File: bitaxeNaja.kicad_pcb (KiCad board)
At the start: 6 copper layers, 65 x 112 mm, 197 parts, among them J1 XT30, J2 Conn_01x08, J3 Conn_01x04, J4 USB_C_Receptacle_USB2.0, J7 Conn_01x04, J8 TC2030-IDC, SW1 SWITCH-SPST, SW2 SWITCH-SPST, U1 TPS546D24ARVFR, U10 BM1370_mode1, U11 MCP1824T-1202E/OT, U12 MCP1824T-0802E, U13 EMC2103-2, U2 SN74AVC4T774, U3 TPSM861253RDXR, U4 TPS546D24ARVFR, U5 L78L05_SOT89, U6 ESP32-S3-WROOM-1, U8 25MHz, U9 BM1370_mode1

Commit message: lots of routing
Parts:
- removed the G*** at (130.5, 70.7)
- removed R10, R12, R9: R, Resistor_SMD:R_0402_1005Metric
- added R41: 38.3k, Resistor_SMD:R_0402_1005Metric, B.Cu at (132.9, 115.1)
- added R42: 20k, Resistor_SMD:R_0402_1005Metric, B.Cu at (131.8, 115.1)
- added R43: 19.1k, Resistor_SMD:R_0402_1005Metric, B.Cu at (129.1, 115.1)
- added R44: 20k, Resistor_SMD:R_0402_1005Metric, B.Cu at (128.0, 115.1)
- A1: renamed from U9; value BM1370_mode1 -> BM1340_mode1; footprint bitaxe:BM1370 -> bitaxe:BM1340
- A2: renamed from U10; value BM1370_mode1 -> BM1340_mode1; footprint bitaxe:BM1370 -> bitaxe:BM1340
- U11: value MCP1824T-1202E/OT -> MCP1824
- U12: value MCP1824T-0802E -> MCP1824
- moved TP27 31.4 mm to (95.7, 55.8)
- moved TP32 30.9 mm to (114.7, 39.3)
- moved TP33 29.2 mm to (110.6, 39.3)
- moved FID1 10.5 mm to (100.4, 32.2)
- moved C88 8.38 mm to (133.5, 121.4), turned to 0 degrees
- moved TP18 8.19 mm to (132.9, 112.3)
- moved C90 7.45 mm to (129.6, 121.3), turned to 0 degrees
- moved TP19 6.76 mm to (129.1, 112.3)
- moved R6 6.31 mm to (126.2, 54.9), turned to 0 degrees
- moved R13 6.27 mm to (146.7, 78.8), turned to 90 degrees
- moved C89 6.21 mm to (134.0, 115.1), turned to -90 degrees
- moved R21 6.13 mm to (126.2, 56.1), turned to 180 degrees
- moved TP4 5.30 mm to (103.8, 110.8)
- moved U11 5.16 mm to (133.0, 118.6), turned to 90 degrees
- moved R11 5.01 mm to (147.9, 78.8), turned to -90 degrees
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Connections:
- U1 pad 29: Net-(U1-MSEL2) -> unconnected-(U1-MSEL2-Pad29)
- U11 pad 4: unconnected-(U11-PG-Pad4) -> Net-(U11-ADJ)
- U12 pad 4: unconnected-(U12-PG-Pad4) -> Net-(U12-ADJ)
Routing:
- net GND: track 98.4 -> 69.7 mm, vias 332 -> 238
- net Net-(U1-MSEL2): track 27.7 -> 0.00 mm, vias 2 -> 0
- net /5V: track 184.2 -> 161.8 mm, vias 9 -> 11
- net /Power/ALRT_VR: track 54.5 -> 66.9 mm, vias 4 -> 3
- net /3V3: track 145.5 -> 134.3 mm
- net /ESP32/IO0: track 91.2 -> 81.9 mm
- net /Power/AGND2: track 30.9 -> 40.1 mm, vias 4 -> 3
- net Net-(U1-VSEL): track 25.8 -> 17.2 mm
- net /ASIC/TEMP2_N: track 36.3 -> 27.8 mm
- net Net-(A1-INV_CLKO): track 14.2 -> 7.18 mm
- net /ASIC/TEMP1_P: track 26.0 -> 33.0 mm
- net Net-(A1-LITE_PAD): track 13.0 -> 6.14 mm
- net /ASIC/TEMP1_N: track 24.6 -> 31.4 mm
- net /ASIC/TEMP2_P: track 33.2 -> 26.4 mm
- net /ASIC/1V2: track 114.9 -> 108.1 mm, vias 7 -> 6
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- removed copper zone on In2.Cu, net /Power/AGND1
- removed copper zone on In2.Cu, net /Power/AGND2
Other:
- board text added: "1200x"
- board text removed: "800xxx"

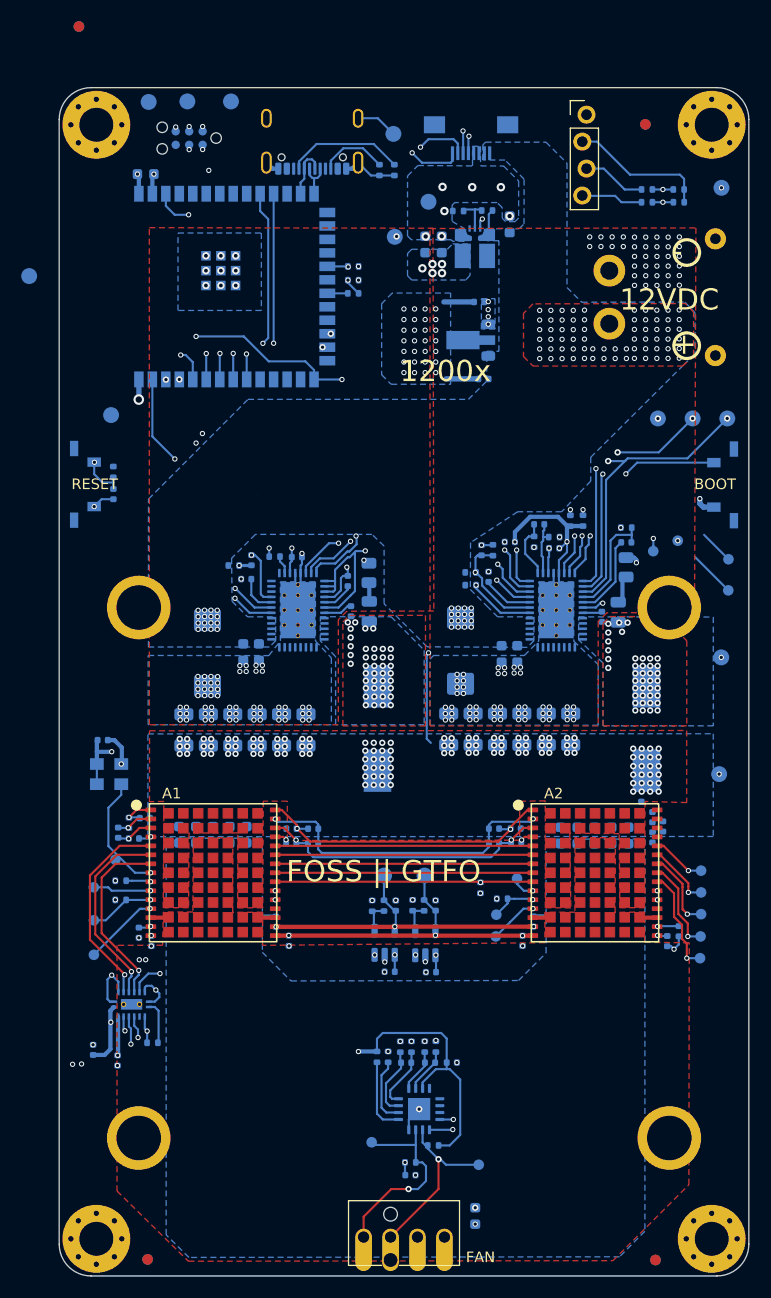
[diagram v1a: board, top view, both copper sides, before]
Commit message: placed and routed and DRC'd. updated TPS546 for 1.0V output.
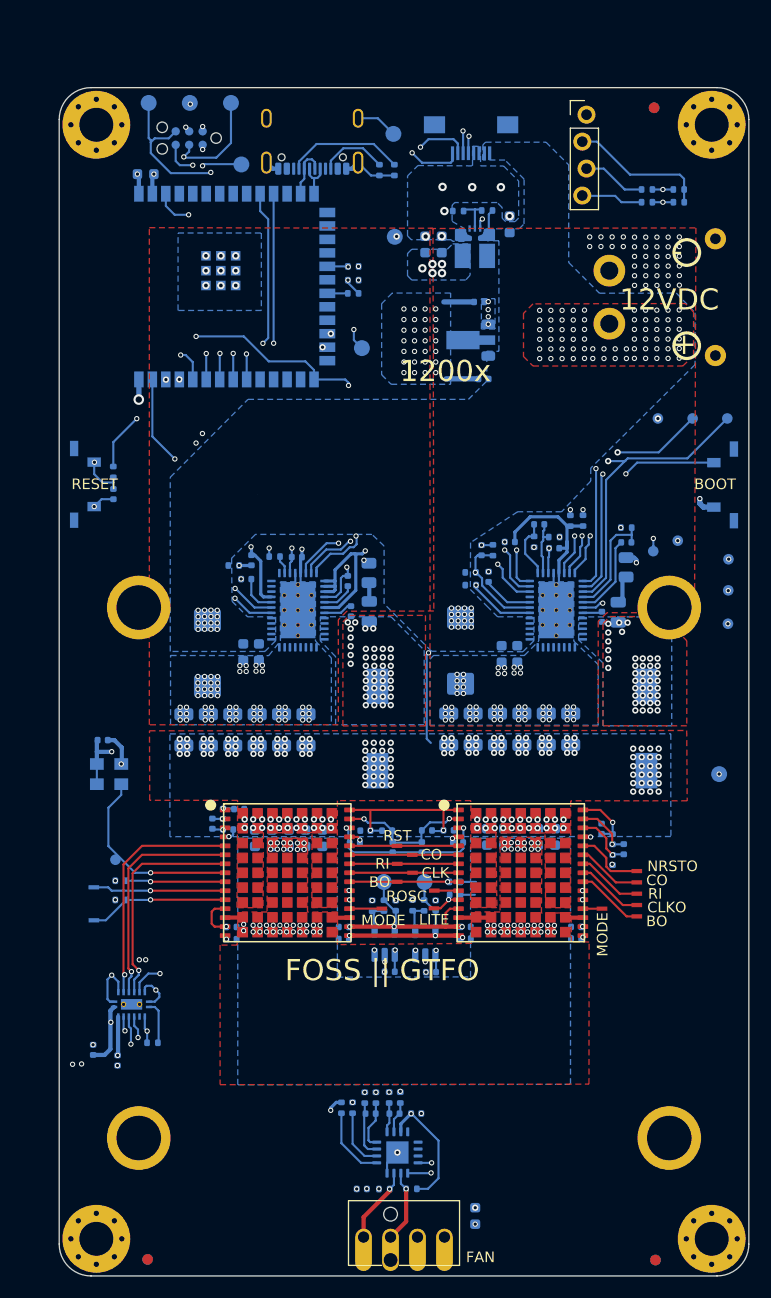
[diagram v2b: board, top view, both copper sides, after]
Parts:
- removed FID1: Fiducial, bitaxe:Fiducial_1mm_Mask2mm
- removed TP14, TP16, TP20, TP21: TestPoint, TestPoint:TestPoint_Pad_D1.0mm
- removed TP17, TP28: GND, TestPoint:TestPoint_Pad_D1.5mm
- added TP26: RST, bitaxe:TestPoint_Pad_1.0x0.4mm, F.Cu at (130.3, 109.5)
- added TP37: CO, bitaxe:TestPoint_Pad_1.0x0.4mm, F.Cu at (131.8, 110.3)
- added TP38: RI, bitaxe:TestPoint_Pad_1.0x0.4mm, F.Cu at (130.4, 111.2)
- added TP39: CLK, bitaxe:TestPoint_Pad_1.0x0.4mm, F.Cu at (131.8, 112.0)
- added TP40: BO, bitaxe:TestPoint_Pad_1.0x0.4mm, F.Cu at (130.4, 112.8)
- added TP41: MODE, bitaxe:TestPoint_Pad_1.0x0.4mm, F.Cu at (128.9, 115.4)
- added TP42: MODE, bitaxe:TestPoint_Pad_1.0x0.4mm, F.Cu at (149.7, 115.4)
- L1, L2: value 300nH -> 230nH; footprint bitaxe:SLC1175-271MEC_COC -> bitaxe:FP1107R1
- R11: value 14.7k -> 46.4k
- R13: value 56.2k -> 31.6k
- R4: value 75k -> 6.04k
- R5: value 10k -> 649
- R7: value 14.7k -> 31.6k
- TP10: value TestPoint -> ROSC; footprint TestPoint:TestPoint_Pad_D1.0mm -> bitaxe:TestPoint_Pad_1.0x0.4mm
- TP11: value TestPoint -> ROSC; footprint TestPoint:TestPoint_Pad_D1.0mm -> bitaxe:TestPoint_Pad_1.0x0.4mm; moved to F.Cu
- TP12: value TestPoint -> LITE; footprint TestPoint:TestPoint_Pad_D1.0mm -> bitaxe:TestPoint_Pad_1.0x0.4mm
- TP13: value TestPoint -> LITE; footprint TestPoint:TestPoint_Pad_D1.0mm -> bitaxe:TestPoint_Pad_1.0x0.4mm; moved to F.Cu
- TP22, TP23, TP24, TP25: footprint TestPoint:TestPoint_Pad_D1.5mm -> TestPoint:TestPoint_Pad_D1.0mm
- TP29: value TestPoint -> EN
- TP32: value TestPoint -> TX
- TP33: value TestPoint -> RX
- TP34: value TestPoint -> 3V3
- TP35: value TestPoint -> GND
- TP36: value TestPoint -> IO0
- TP5, TP6, TP7, TP8, TP9: footprint TestPoint:TestPoint_Pad_D1.0mm -> bitaxe:TestPoint_Pad_1.0x0.4mm; moved to F.Cu
- moved TP25 41.1 mm to (161.5, 88.5)
- moved TP27 32.1 mm to (127.0, 62.5)
- moved TP29 26.6 mm to (115.7, 45.2)
- moved C87 9.69 mm to (147.2, 117.1), turned to 0 degrees
- moved C66 8.92 mm to (114.0, 106.4)
- moved C64 8.92 mm to (114.4, 107.9)
- moved C65 8.92 mm to (112.9, 107.4)
- moved C67 8.92 mm to (115.5, 106.0)
- moved C80 8.75 mm to (114.7, 117.1), turned to 180 degrees
- moved C86 8.59 mm to (147.2, 118.2), turned to 0 degrees
- moved TP11 7.88 mm to (133.8, 113.7)
- moved C81 7.56 mm to (114.7, 118.3), turned to 180 degrees
- moved C70 7.51 mm to (129.9, 109.6), turned to -90 degrees
- moved C54 7.16 mm to (121.7, 108.7)
- moved C55 7.16 mm to (120.1, 108.7)
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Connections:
- A1 pad 12: Net-(A1-INV_CLKO) -> /ASIC/0V8_1
- A1 pad 19: unconnected-(A1-PIN_MODE-Pad19) -> Net-(A1-PIN_MODE)
- A2 pad 12: Net-(A2-INV_CLKO) -> /ASIC/0V8
- A2 pad 19: unconnected-(A2-PIN_MODE-Pad19) -> Net-(A2-PIN_MODE)
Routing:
- net Net-(A1-VDD2_1): track 29.3 -> 13.6 mm
- net /ASIC/1V2: track 108.1 -> 94.0 mm
- net Net-(A1-RI): track 24.3 -> 10.3 mm
- net Net-(A1-NRSTO): track 24.3 -> 10.3 mm
- net Net-(A1-CO): track 24.3 -> 10.3 mm
- net Net-(A1-CLKO): track 24.3 -> 10.3 mm
- net Net-(A1-BO): track 24.3 -> 10.5 mm
- net Net-(A1-VDD3_1): track 29.3 -> 16.3 mm
- net Net-(A1-VDD1_1): track 27.1 -> 15.0 mm
- net /fan/FAN_PWM: track 19.0 -> 7.22 mm
- net /ASIC/0V8: track 30.0 -> 18.4 mm
- net /fan/FAN_TACH: track 16.8 -> 6.84 mm
- net /ESP32/P_RX: track 21.5 -> 30.8 mm, vias 2 -> 3
- net /ESP32/P_TX: track 24.6 -> 32.2 mm
- net /ESP32/IO0: track 81.9 -> 89.2 mm
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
